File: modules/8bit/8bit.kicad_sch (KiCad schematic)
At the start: 24 parts, among them SW1 MODE SELECT, U1 MCP6002-xSN, U2 ATtiny1616-M, U3 MCP6002-xSN

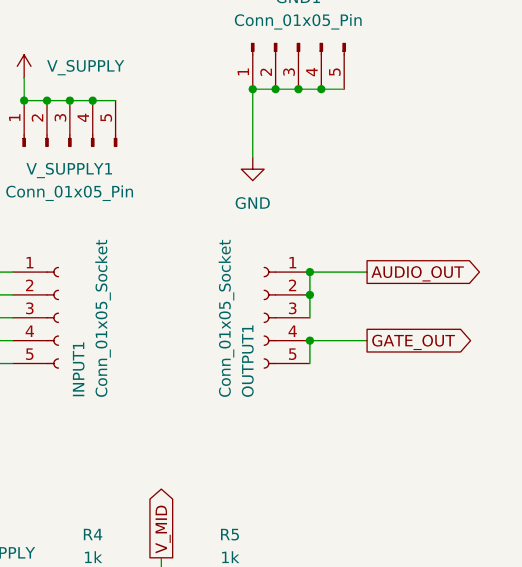
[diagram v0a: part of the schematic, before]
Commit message: 8bit: Add MIDI THRU support
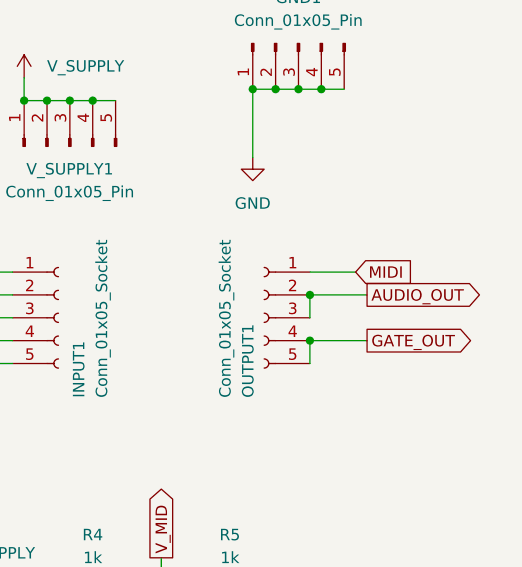
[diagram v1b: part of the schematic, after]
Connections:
- net AUDIO_OUT: no longer OUTPUT1.1 (Pin_1)
- net MIDI: now also OUTPUT1.1 (Pin_1)
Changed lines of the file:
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@@
+	)
+	(junction
+		(at 355.6 31.75)
+		(diameter 0)
+		(color 0 0 0 0)
+	)
+	(junction
+		(at 381 30.48)
+		(diameter 0)
+		(color 0 0 0 0)
+	)
+	(junction
+		(at 363.22 86.36)
+		(diameter 0)
+		(color 0 0 0 0)
+	)
+	(junction
+		(at 379.73 58.42)
+		(diameter 0)
+		(color 0 0 0 0)
+	)
+	(junction
+		(at 378.46 30.48)
+		(diameter 0)
+		(color 0 0 0 0)
+	)
+	(junction
+		(at 375.92 134.62)
+		(diameter 0)
+		(color 0 0 0 0)
+	)
+	(junction
+		(at 85.09 198.12)
+		(diameter 0)
+		(color 0 0 0 0)
+	)
+	(junction
+		(at 44.45 146.05)
+		(diameter 0)
+		(color 0 0 0 0)
+	)
+	(junction
+		(at 218.44 73.66)
+		(diameter 0)
+		(color 0 0 0 0)
+	)
+	(junction
+		(at 353.06 31.75)
+		(diameter 0)
+		(color 0 0 0 0)
 	)
 	(junction
@@
 	)
 	(junction
-		(at 355.6 31.75)
-		(diameter 0)
-		(color 0 0 0 0)
-	)
-	(junction
-		(at 381 30.48)
-		(diameter 0)
-		(color 0 0 0 0)
-	)
-	(junction
-		(at 363.22 86.36)
-		(diameter 0)
-		(color 0 0 0 0)
-	)
-	(junction
-		(at 379.73 58.42)
-		(diameter 0)
-		(color 0 0 0 0)
-	)
-	(junction
-		(at 378.46 30.48)
-		(diameter 0)
-		(color 0 0 0 0)
-	)
-	(junction
-		(at 375.92 134.62)
-		(diameter 0)
-		(color 0 0 0 0)
-	)
-	(junction
-		(at 85.09 198.12)
-		(diameter 0)
-		(color 0 0 0 0)
-	)
-	(junction
-		(at 44.45 146.05)
-		(diameter 0)
-		(color 0 0 0 0)
-	)
-	(junction
-		(at 218.44 73.66)
-		(diameter 0)
-		(color 0 0 0 0)
-	)
-	(junction
-		(at 353.06 31.75)
-		(diameter 0)
-		(color 0 0 0 0)
-	)
-	(junction
 		(at 345.44 135.89)
 		(diameter 0)
@@
 	)
 	(junction
-		(at 379.73 50.8)
-		(diameter 0)
-		(color 0 0 0 0)
-	)
-	(junction
 		(at 92.71 39.37)
 		(diameter 0)
@@
 	(wire
 		(pts
+			(xy 379.73 53.34) (xy 386.08 53.34)
+		)
+		(stroke
+			(width 0)
+			(type default)
+		)
+	)
+	(wire
+		(pts
 			(xy 363.22 82.55) (xy 363.22 86.36)
 		)
@@
 	(wire
 		(pts
-			(xy 379.73 50.8) (xy 379.73 53.34)
-		)
-		(stroke
-			(width 0)
-			(type default)
-		)
-	)
-	(wire
-		(pts
 			(xy 44.45 185.42) (xy 44.45 186.69)
 		)
@@
 	(wire
 		(pts
-			(xy 379.73 50.8) (xy 386.08 50.8)
+			(xy 379.73 50.8) (xy 384.81 50.8)
 		)
 		(stroke
@@
 	(global_label "AUDIO_OUT"
 		(shape output)
-		(at 386.08 50.8 0)
+		(at 386.08 53.34 0)
 		(fields_autoplaced yes)
 		(effects
@@
 		)
 		(property "Intersheetrefs" "${INTERSHEET_REFS}"
-			(at 399.2858 50.8 0)
+			(at 399.2858 53.34 0)
 			(effects
 				(font
@@
 			(effects
 				(font
+					(size 1.27 1.27)
+				)
+				(justify left)
+				(hide yes)
+			)
+		)
+	)
+	(global_label "MIDI"
+		(shape input)
+		(at 384.81 50.8 0)
+		(fields_autoplaced yes)
+		(effects
+			(font
+				(size 1.27 1.27)
+			)
+			(justify left)
+		)
+		(property "Intersheetrefs" "${INTERSHEET_REFS}"
+			(at 391.7262 50.8 0)
+			(effects
+				(font

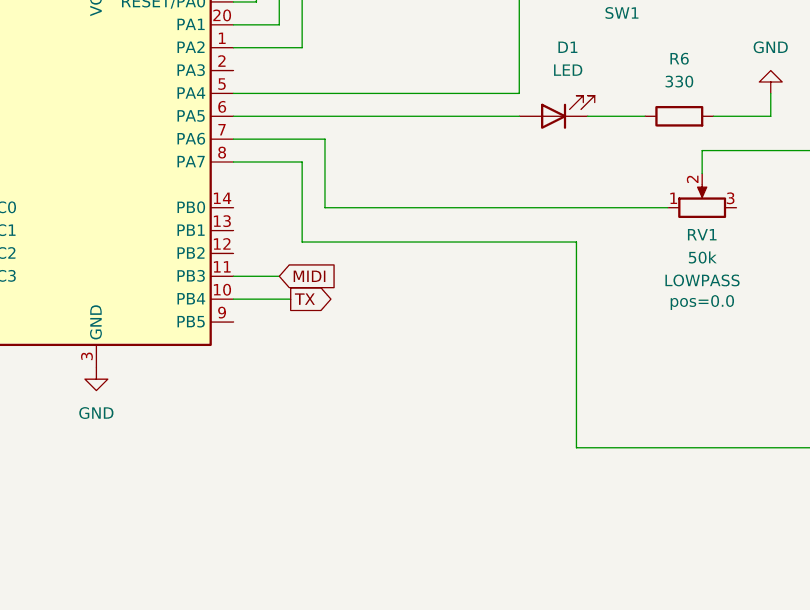
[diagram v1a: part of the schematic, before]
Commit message: 8bit: Use PB2 as the serial port We used a Software Serial earlier and it uses some memory and flash where we could use somewhere else. Now we go back to the Serial port.
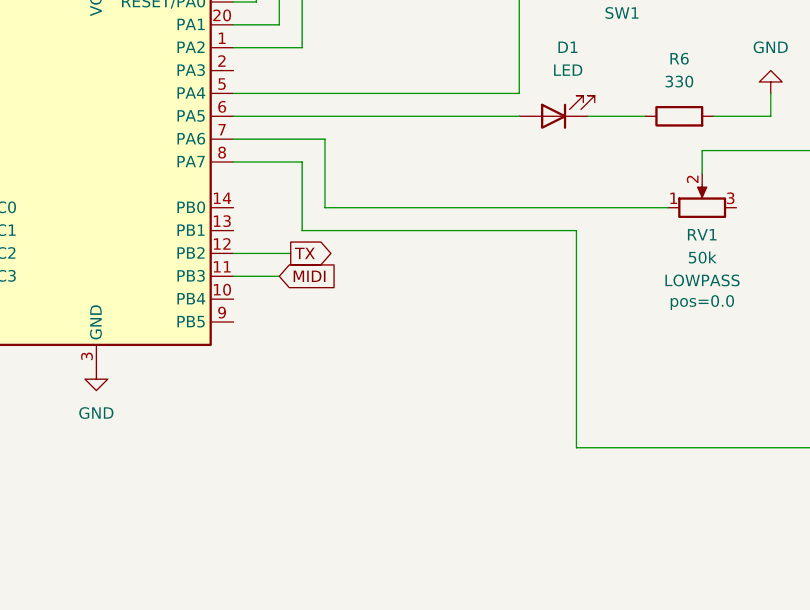
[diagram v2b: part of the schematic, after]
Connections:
- net TX: now also U2.12 (PB2); no longer U2.10 (PB4)
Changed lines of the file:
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@@
 	(wire
 		(pts
-			(xy 115.57 81.28) (xy 115.57 72.39)
+			(xy 115.57 80.01) (xy 115.57 72.39)
 		)
 		(stroke
@@
 	(wire
 		(pts
-			(xy 146.05 81.28) (xy 146.05 104.14)
+			(xy 146.05 80.01) (xy 146.05 104.14)
 		)
 		(stroke
@@
 	(wire
 		(pts
+			(xy 107.95 82.55) (xy 114.3 82.55)
+		)
+		(stroke
+			(width 0)
+			(type default)
+		)
+	)
+	(wire
+		(pts
 			(xy 375.92 137.16) (xy 375.92 134.62)
 		)
@@
 	(wire
 		(pts
-			(xy 107.95 87.63) (xy 114.3 87.63)
-		)
-		(stroke
-			(width 0)
-			(type default)
-		)
-	)
-	(wire
-		(pts
 			(xy 85.09 198.12) (xy 85.09 208.28)
 		)
@@
 	(wire
 		(pts
-			(xy 146.05 81.28) (xy 115.57 81.28)
+			(xy 146.05 80.01) (xy 115.57 80.01)
 		)
 		(stroke
@@
 	(global_label "TX"
 		(shape output)
-		(at 114.3 87.63 0)
+		(at 114.3 82.55 0)
 		(fields_autoplaced yes)
 		(effects
@@
 		)
 		(property "Intersheetrefs" "${INTERSHEET_REFS}"
-			(at 119.4623 87.63 0)
-			(effects
-				(font
+			(at 119.4623 82.55 0)
+			(effects
+				(font

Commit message: 8bit: Change the push button
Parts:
- SW1: footprint BreadModular_MISC:SPST_TS-1187A-B-A-B -> BreadModular_MISC:K2-1808SN-A4SW-01
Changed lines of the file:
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@@
 			)
 		)
-		(property "Footprint" "BreadModular_MISC:SPST_TS-1187A-B-A-B"
+		(property "Footprint" "BreadModular_MISC:K2-1808SN-A4SW-01"
 			(at 151.13 49.53 0)
 			(effects
